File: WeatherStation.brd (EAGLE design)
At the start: 30.5 x 53.3 mm, 18 parts, among them J1 EDISON_CONNECTOR_FULLMOUNTING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, J2 EDISON_CONNECTOR_FULLHEADER, U1 MCP73831

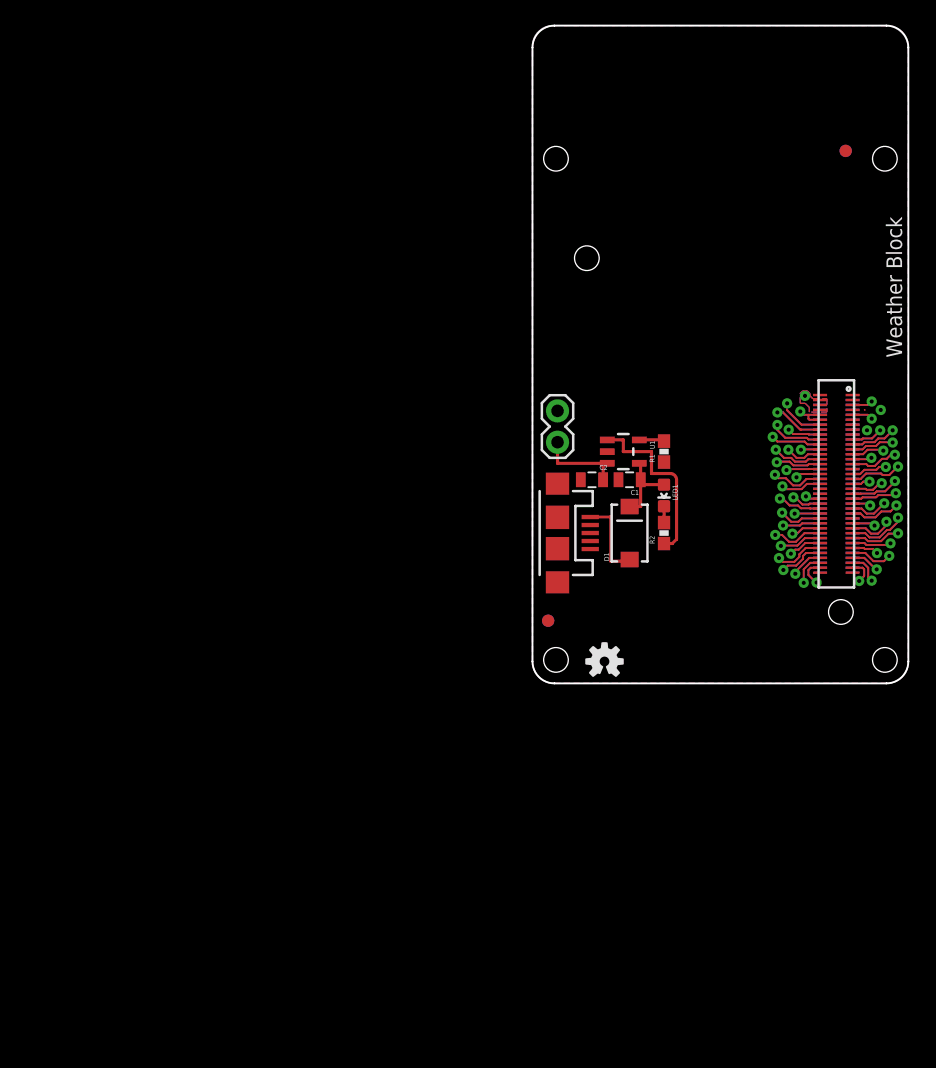
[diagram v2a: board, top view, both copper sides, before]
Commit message: placed HTU21D, MPL3115A2, MIC5205-3.3V, PCA9306
RH/temp, barometric pressure/temp, LDO voltage regulator and 1.8-3.3V
logic level shifter.
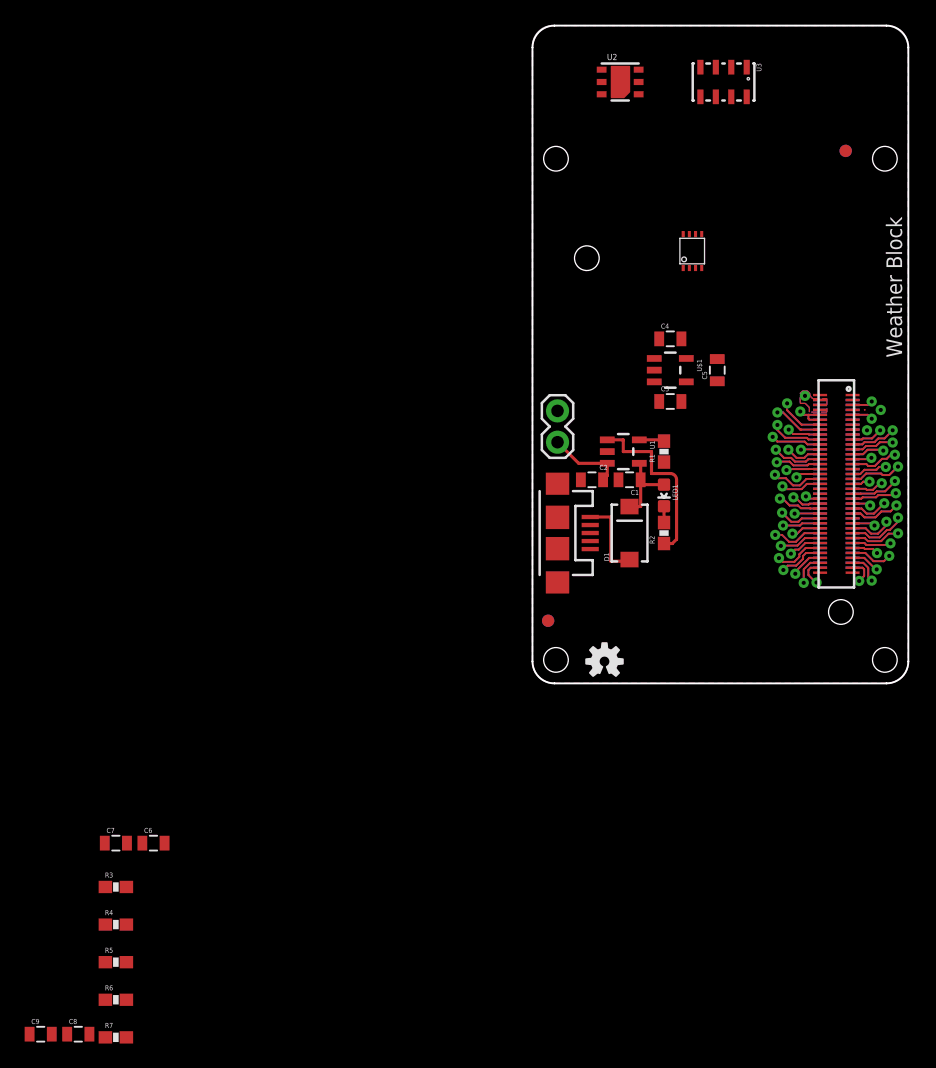
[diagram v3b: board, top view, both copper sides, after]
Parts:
- added C3, C4, C5, C6, C7, C8, C9: 4.7µF, SparkFun-Capacitors:0805
- added R3, R4, R5, R6, R7: 330Ω, SparkFun-Resistors:0603-RES
- added U$1: 3.3V/150mA, SparkFun-PowerIC:SOT23-5
- added U2: HTU21DSMD, SparkFun-Sensors:HTU21D
- added U3: MPL3115A2LGA8, SparkFun-Sensors:LGA8
- added U4: PCA9306, SparkFun-DigitalIC:PSOP-8
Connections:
- new net CAP: U3.2
- new net N$7: C3.1, U$1.1, U$1.3
- new net N$8: C5.1, U$1.4
- new net VDD: U2.VDD, U3.1
- net 3.3V: now also C4.1, U$1.5
- net GND: now also C3.2, C4.2, C5.2, U$1.2, U2.7, U2.GND, U3.3, U3.4, U4.4
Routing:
- net VBAT: track 7.08 -> 6.22 mm
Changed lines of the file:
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@@
 <element name="R2" library="SparkFun-Resistors" package="0603-RES" value="330Ω" x="10.668" y="12.192" rot="R90"/>
 <element name="JP2" library="SparkFun-Connectors" package="1X02" value="M02PTH" x="2.032" y="22.098" smashed="yes" rot="R270"/>
+<element name="U2" library="SparkFun-Sensors" package="HTU21D" value="HTU21DSMD" x="7.112" y="48.768"/>
+<element name="U3" library="SparkFun-Sensors" package="LGA8" value="MPL3115A2LGA8" x="15.494" y="48.768" rot="R270"/>
+<element name="U4" library="SparkFun-DigitalIC" package="PSOP-8" value="PCA9306" x="12.954" y="35.052">
+<attribute name="PROD_ID" value="IC-10023" x="12.954" y="35.052" size="1.778" layer="27" display="off"/>
+</element>
+<element name="U$1" library="SparkFun-PowerIC" package="SOT23-5" value="3.3V/150mA" x="11.176" y="25.4" rot="R270">
+<attribute name="PROD_ID" value="VREG-00822" x="11.176" y="25.4" size="1.778" layer="27" rot="R270" display="off"/>
+</element>
+<element name="C3" library="SparkFun-Capacitors" package="0805" value="4.7µF" x="11.176" y="22.86"/>
+<element name="C4" library="SparkFun-Capacitors" package="0805" value="4.7µF" x="11.176" y="27.94"/>
+<element name="C5" library="SparkFun-Capacitors" package="0805" value="4.7µF" x="14.986" y="25.4" rot="R90"/>
+<element name="C6" library="SparkFun-Capacitors" package="0805" value="4.7µF" x="-30.734" y="-12.954"/>
+<element name="C7" library="SparkFun-Capacitors" package="0805" value="4.7µF" x="-33.782" y="-12.954"/>
+<element name="R3" library="SparkFun-Resistors" package="0603-RES" value="330Ω" x="-33.782" y="-16.51"/>
+<element name="R4" library="SparkFun-Resistors" package="0603-RES" value="330Ω" x="-33.782" y="-19.558"/>
+<element name="R5" library="SparkFun-Resistors" package="0603-RES" value="330Ω" x="-33.782" y="-22.606"/>
+<element name="R6" library="SparkFun-Resistors" package="0603-RES" value="330Ω" x="-33.782" y="-25.654"/>
+<element name="R7" library="SparkFun-Resistors" package="0603-RES" value="330Ω" x="-33.782" y="-28.702"/>
+<element name="C8" library="SparkFun-Capacitors" package="0805" value="4.7µF" x="-36.83" y="-28.448"/>
+<element name="C9" library="SparkFun-Capacitors" package="0805" value="4.7µF" x="-39.878" y="-28.448"/>
 </elements>
 <signals>
@@
 <contactref element="U1" pad="2"/>
 <contactref element="JP2" pad="1"/>
+<contactref element="U2" pad="GND"/>
+<contactref element="U2" pad="7"/>
+<contactref element="U3" pad="3"/>
+<contactref element="U4" pad="4"/>
+<contactref element="U3" pad="4"/>
+<contactref element="U$1" pad="2"/>
+<contactref element="C3" pad="2"/>
+<contactref element="C4" pad="2"/>
+<contactref element="C5" pad="2"/>
+<wire x1="13.619" y1="49.968" x2="14.869" y2="49.968" width="0" layer="19" extent="1-1"/>
+<wire x1="8.612" y1="48.768" x2="13.619" y2="49.968" width="0" layer="19" extent="1-1"/>
+<wire x1="7.112" y1="48.768" x2="8.612" y2="48.768" width="0" layer="19" extent="1-1"/>
+<wire x1="13.724" y1="33.682" x2="8.612" y2="48.768" width="0" layer="19" extent="1-1"/>
+<wire x1="9.8759" y1="25.4" x2="13.724" y2="33.682" width="0" layer="19" extent="1-1"/>
+<wire x1="10.668" y1="17.946" x2="9.8759" y2="25.4" width="0" layer="19" extent="1-1"/>
+<wire x1="6.974" y1="16.51" x2="10.668" y2="17.946" width="0" layer="19" extent="1-1"/>
+<wire x1="6.0659" y1="18.796" x2="6.974" y2="16.51" width="0" layer="19" extent="1-1"/>
+<wire x1="3.926" y1="16.51" x2="6.974" y2="16.51" width="0" layer="19" extent="1-1"/>
+<wire x1="2.032" y1="16.192" x2="3.926" y2="16.51" width="0" layer="19" extent="1-1"/>
+<wire x1="2.032" y1="22.098" x2="6.0659" y2="18.796" width="0" layer="19" extent="1-1"/>
+<wire x1="4.682" y1="10.892" x2="3.926" y2="16.51" width="0" layer="19" extent="1-1"/>
+<wire x1="2.032" y1="8.192" x2="4.682" y2="10.892" width="0" layer="19" extent="1-1"/>
+<wire x1="25.96" y1="22.98" x2="9.8759" y2="25.4" width="0" layer="19" extent="1-16"/>
+<wire x1="25.96" y1="22.9798" x2="25.96" y2="22.98" width="0" layer="19" extent="1-16"/>
+<wire x1="25.96" y1="22.18" x2="25.96" y2="22.98" width="0" layer="19" extent="16-16"/>
+<wire x1="25.96" y1="22.1798" x2="25.96" y2="22.18" width="0" layer="19" extent="1-16"/>
+<wire x1="25.96" y1="21.38" x2="25.96" y2="22.18" width="0" layer="19" extent="16-16"/>
+<wire x1="25.96" y1="21.3798" x2="25.96" y2="21.38" width="0" layer="19" extent="1-16"/>
+<wire x1="25.96" y1="20.98" x2="25.96" y2="21.38" width="0" layer="19" extent="16-16"/>
+<wire x1="25.96" y1="20.9798" x2="25.96" y2="20.98" width="0" layer="19" extent="1-16"/>
+<wire x1="25.96" y1="20.58" x2="25.96" y2="20.98" width="0" layer="19" extent="16-16"/>
+<wire x1="25.96" y1="20.5798" x2="25.96" y2="20.58" width="0" layer="19" extent="1-16"/>
+<wire x1="25.96" y1="20.18" x2="25.96" y2="20.58" width="0" layer="19" extent="16-16"/>
+<wire x1="25.96" y1="20.1798" x2="25.96" y2="20.18" width="0" layer="19" extent="1-16"/>
+<wire x1="26.9438" y1="22.1798" x2="25.96" y2="22.18" width="0" layer="19" extent="1-16"/>
+<wire x1="27.1272" y1="20.5232" x2="25.96" y2="20.58" width="0" layer="19" extent="16-16"/>
+<wire x1="28.2448" y1="22.1742" x2="26.9438" y2="22.1798" width="0" layer="19" extent="1-1"/>
+<wire x1="12.076" y1="22.86" x2="2.032" y2="8.192" width="0" layer="19" extent="1-1"/>
+<wire x1="12.076" y1="27.94" x2="12.076" y2="22.86" width="0" layer="19" extent="1-1"/>
+<wire x1="14.986" y1="26.3" x2="12.076" y2="27.94" width="0" layer="19" extent="1-1"/>
 </signal>
 <signal name="VSYS">
@@
 <wire x1="22.4604" y1="21.38" x2="22.3774" y2="21.463" width="0.1524" layer="16"/>
 <wire x1="22.3774" y1="21.463" x2="22.3774" y2="21.78" width="0.1524" layer="16"/>
+<contactref element="U$1" pad="5"/>
+<contactref element="C4" pad="1"/>
+<wire x1="12.4761" y1="26.35" x2="10.276" y2="27.94" width="0" layer="19" extent="1-1"/>
+<wire x1="21.717" y1="22.0472" x2="12.4761" y2="26.35" width="0" layer="19" extent="1-1"/>
 </signal>
 <signal name="GP183_PWM3">
@@
 <contactref element="C2" pad="1"/>
 <contactref element="JP2" pad="2"/>
-<wire x1="6.0659" y1="17.846" x2="5.726" y2="17.846" width="0.254" layer="1"/>
-<wire x1="5.726" y1="17.846" x2="5.726" y2="16.51" width="0.254" layer="1"/>
-<wire x1="5.726" y1="17.846" x2="2.032" y2="17.846" width="0.254" layer="1"/>
-<wire x1="2.032" y1="17.846" x2="2.032" y2="19.558" width="0.254" layer="1"/>
+<wire x1="6.0659" y1="17.846" x2="6.0659" y2="16.8499" width="0.254" layer="1"/>
+<wire x1="6.0659" y1="16.8499" x2="5.726" y2="16.51" width="0.254" layer="1"/>
+<wire x1="6.0659" y1="17.846" x2="3.744" y2="17.846" width="0.254" layer="1"/>
+<wire x1="3.744" y1="17.846" x2="2.032" y2="19.558" width="0.254" layer="1"/>
 </signal>
 <signal name="N$6">
@@
 <wire x1="10.668" y1="19.746" x2="10.668" y2="19.646" width="0.254" layer="1"/>
 </signal>
+<signal name="VDD">
+<contactref element="U2" pad="VDD"/>
+<contactref element="U3" pad="1"/>
+<wire x1="17.369" y1="49.968" x2="5.612" y2="48.768" width="0" layer="19" extent="1-1"/>
+</signal>
+<signal name="CAP">
+<contactref element="U3" pad="2"/>
+</signal>
+<signal name="N$7">
+<contactref element="U$1" pad="3"/>
+<contactref element="U$1" pad="1"/>
+<contactref element="C3" pad="1"/>
+<wire x1="9.8759" y1="26.35" x2="10.276" y2="22.86" width="0" layer="19" extent="1-1"/>
+<wire x1="9.8759" y1="24.45" x2="9.8759" y2="26.35" width="0" layer="19" extent="1-1"/>
+</signal>
+<signal name="N$8">
+<contactref element="U$1" pad="4"/>
+<contactref element="C5" pad="1"/>
+<wire x1="12.4761" y1="24.45" x2="14.986" y2="24.5" width="0" layer="19" extent="1-1"/>
+</signal>
 </signals>

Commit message: connected schematic for HTU21D
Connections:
- new net SCL: U2.SCK
- new net SDA: U2.DATA
- net 3.3V: now also C8.1, U2.VDD
- net GND: now also C8.2
- net VDD: no longer U2.VDD
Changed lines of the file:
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@@
 <contactref element="C4" pad="2"/>
 <contactref element="C5" pad="2"/>
-<wire x1="13.619" y1="49.968" x2="14.869" y2="49.968" width="0" layer="19" extent="1-1"/>
-<wire x1="8.612" y1="48.768" x2="13.619" y2="49.968" width="0" layer="19" extent="1-1"/>
-<wire x1="7.112" y1="48.768" x2="8.612" y2="48.768" width="0" layer="19" extent="1-1"/>
-<wire x1="13.724" y1="33.682" x2="8.612" y2="48.768" width="0" layer="19" extent="1-1"/>
-<wire x1="9.8759" y1="25.4" x2="13.724" y2="33.682" width="0" layer="19" extent="1-1"/>
-<wire x1="10.668" y1="17.946" x2="9.8759" y2="25.4" width="0" layer="19" extent="1-1"/>
-<wire x1="6.974" y1="16.51" x2="10.668" y2="17.946" width="0" layer="19" extent="1-1"/>
+<contactref element="C8" pad="2"/>
+<wire x1="2.032" y1="8.192" x2="-35.93" y2="-28.448" width="0" layer="19" extent="1-1"/>
+<wire x1="4.682" y1="10.892" x2="2.032" y2="8.192" width="0" layer="19" extent="1-1"/>
+<wire x1="3.926" y1="16.51" x2="4.682" y2="10.892" width="0" layer="19" extent="1-1"/>
+<wire x1="2.032" y1="16.192" x2="3.926" y2="16.51" width="0" layer="19" extent="1-1"/>
+<wire x1="6.974" y1="16.51" x2="3.926" y2="16.51" width="0" layer="19" extent="1-1"/>
 <wire x1="6.0659" y1="18.796" x2="6.974" y2="16.51" width="0" layer="19" extent="1-1"/>
-<wire x1="3.926" y1="16.51" x2="6.974" y2="16.51" width="0" layer="19" extent="1-1"/>
-<wire x1="2.032" y1="16.192" x2="3.926" y2="16.51" width="0" layer="19" extent="1-1"/>
+<wire x1="10.668" y1="17.946" x2="6.974" y2="16.51" width="0" layer="19" extent="1-1"/>
+<wire x1="12.076" y1="22.86" x2="10.668" y2="17.946" width="0" layer="19" extent="1-1"/>
+<wire x1="9.8759" y1="25.4" x2="12.076" y2="22.86" width="0" layer="19" extent="1-1"/>
+<wire x1="12.076" y1="27.94" x2="9.8759" y2="25.4" width="0" layer="19" extent="1-1"/>
+<wire x1="14.986" y1="26.3" x2="12.076" y2="27.94" width="0" layer="19" extent="1-1"/>
 <wire x1="2.032" y1="22.098" x2="6.0659" y2="18.796" width="0" layer="19" extent="1-1"/>
-<wire x1="4.682" y1="10.892" x2="3.926" y2="16.51" width="0" layer="19" extent="1-1"/>
-<wire x1="2.032" y1="8.192" x2="4.682" y2="10.892" width="0" layer="19" extent="1-1"/>
-<wire x1="25.96" y1="22.98" x2="9.8759" y2="25.4" width="0" layer="19" extent="1-16"/>
+<wire x1="13.724" y1="33.682" x2="12.076" y2="27.94" width="0" layer="19" extent="1-1"/>
+<wire x1="25.96" y1="22.98" x2="14.986" y2="26.3" width="0" layer="19" extent="1-16"/>
 <wire x1="25.96" y1="22.9798" x2="25.96" y2="22.98" width="0" layer="19" extent="1-16"/>
 <wire x1="25.96" y1="22.18" x2="25.96" y2="22.98" width="0" layer="19" extent="16-16"/>
@@
 <wire x1="27.1272" y1="20.5232" x2="25.96" y2="20.58" width="0" layer="19" extent="16-16"/>
 <wire x1="28.2448" y1="22.1742" x2="26.9438" y2="22.1798" width="0" layer="19" extent="1-1"/>
-<wire x1="12.076" y1="22.86" x2="2.032" y2="8.192" width="0" layer="19" extent="1-1"/>
-<wire x1="12.076" y1="27.94" x2="12.076" y2="22.86" width="0" layer="19" extent="1-1"/>
-<wire x1="14.986" y1="26.3" x2="12.076" y2="27.94" width="0" layer="19" extent="1-1"/>
+<wire x1="8.612" y1="48.768" x2="13.724" y2="33.682" width="0" layer="19" extent="1-1"/>
+<wire x1="7.112" y1="48.768" x2="8.612" y2="48.768" width="0" layer="19" extent="1-1"/>
+<wire x1="13.619" y1="49.968" x2="8.612" y2="48.768" width="0" layer="19" extent="1-1"/>
+<wire x1="14.869" y1="49.968" x2="13.619" y2="49.968" width="0" layer="19" extent="1-1"/>
 </signal>
 <signal name="VSYS">
@@
 <contactref element="U$1" pad="5"/>
 <contactref element="C4" pad="1"/>
+<contactref element="U2" pad="VDD"/>
+<contactref element="C8" pad="1"/>
+<wire x1="10.276" y1="27.94" x2="-37.73" y2="-28.448" width="0" layer="19" extent="1-1"/>
 <wire x1="12.4761" y1="26.35" x2="10.276" y2="27.94" width="0" layer="19" extent="1-1"/>
 <wire x1="21.717" y1="22.0472" x2="12.4761" y2="26.35" width="0" layer="19" extent="1-1"/>
+<wire x1="5.612" y1="48.768" x2="10.276" y2="27.94" width="0" layer="19" extent="1-1"/>
 </signal>
 <signal name="GP183_PWM3">
@@
 </signal>
 <signal name="VDD">
-<contactref element="U2" pad="VDD"/>
 <contactref element="U3" pad="1"/>
-<wire x1="17.369" y1="49.968" x2="5.612" y2="48.768" width="0" layer="19" extent="1-1"/>
 </signal>
 <signal name="CAP">
@@
 <wire x1="12.4761" y1="24.45" x2="14.986" y2="24.5" width="0" layer="19" extent="1-1"/>
 </signal>
+<signal name="SDA">
+<contactref element="U2" pad="DATA"/>
+</signal>
+<signal name="SCL">
+<contactref element="U2" pad="SCK"/>
+</signal>
 </signals>

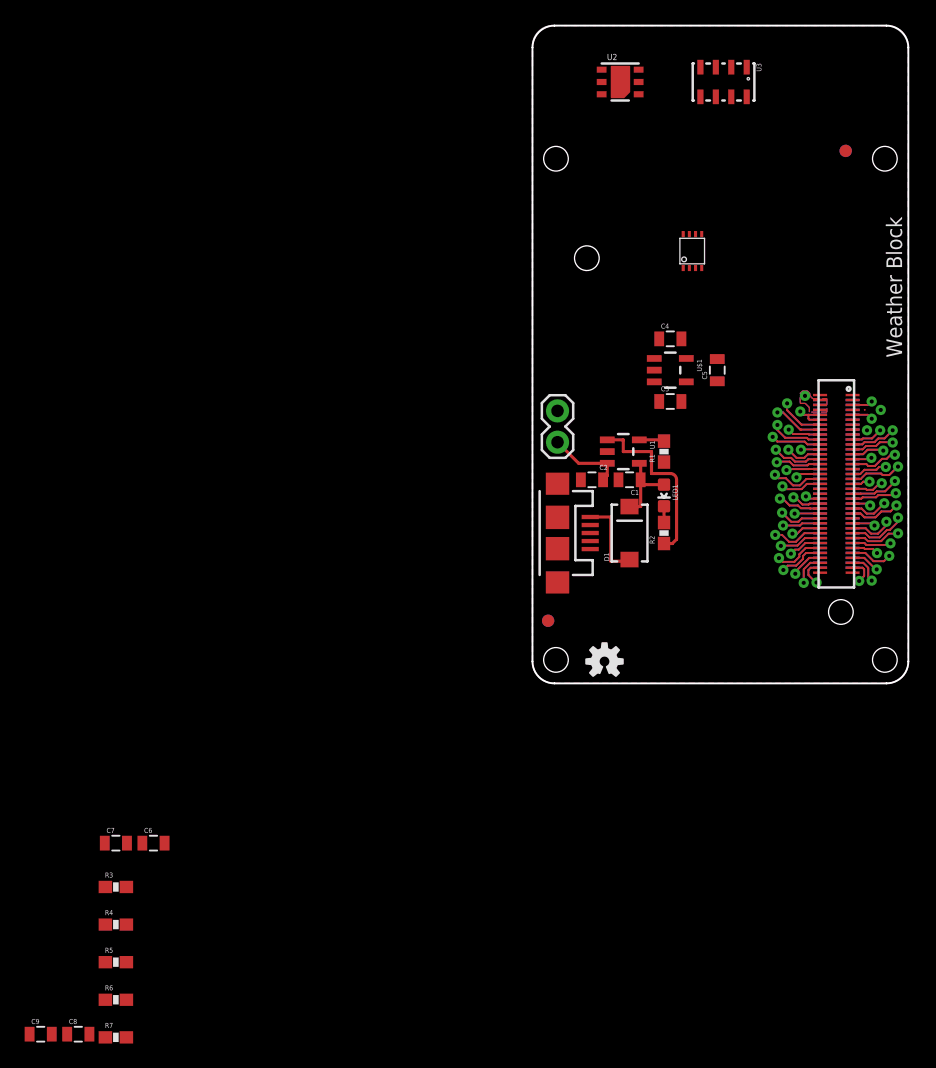
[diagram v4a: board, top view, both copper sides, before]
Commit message: connected schematic for MPL3115A2 and traces for HTU21D
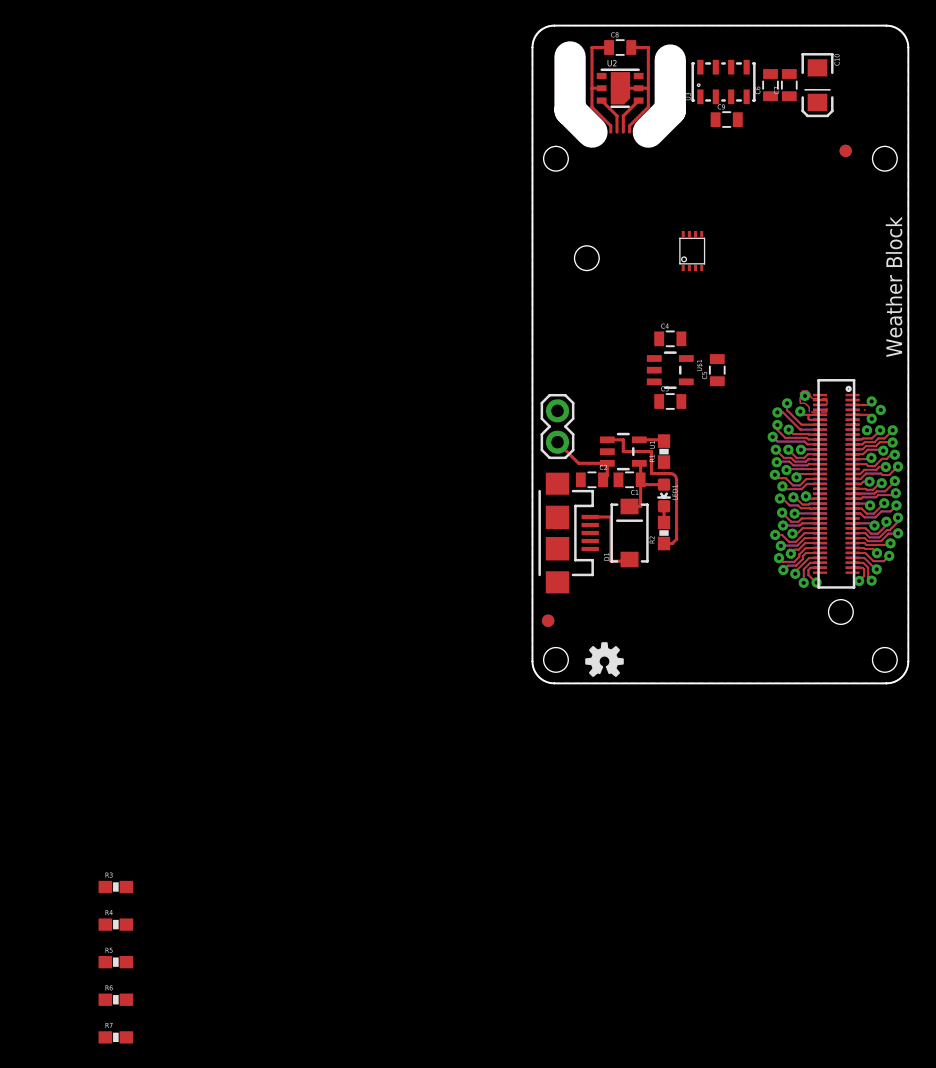
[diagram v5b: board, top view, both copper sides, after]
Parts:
- added C10: 10µF, SparkFun-Capacitors:EIA3216
- C6, C9: value 4.7µF -> 0.1µF
- C7: value 4.7µF -> 1µF
- moved C9 92.7 mm to (15.7, 45.7)
- moved C8 91.3 mm to (7.11, 51.6)
- moved C7 82.2 mm to (20.8, 48.5), turned to 90 degrees
- moved C6 79.3 mm to (19.3, 48.5), turned to 90 degrees
- moved U2 0.51 mm to (7.11, 48.3)
- turned U3 to 90 degrees
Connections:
- removed net CAP: U3.2
- removed net VDD: U3.1
- new net N$10: U3.7
- new net N$3: C9.1, U3.2
- new net N$9: U3.8
- net 3.3V: now also C10.A, C6.1, C7.1, U3.1, U3.4
- net GND: now also C10.C, C6.2, C7.2, C9.2; no longer U3.4
- net SCL: now also U4.2
- net SDA: now also U4.3
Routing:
- net GND: track 0.01 -> 11.2 mm
- net 3.3V: track 6.02 -> 15.7 mm
- net SDA: track 0.00 -> 3.07 mm
- net SCL: track 0.00 -> 3.07 mm
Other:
- outline, holes or cut-outs redrawn
